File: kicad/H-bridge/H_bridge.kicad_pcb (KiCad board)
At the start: 2 copper layers, 127 x 63.5 mm, 69 parts, among them J1 Screw_Terminal_01x03, J2 Conn_Coaxial, J3 2453710000, J4 Screw_Terminal_01x02, Q1 IAUT300N10S5N014ATMA1, Q2 IAUT300N10S5N014ATMA1, Q3 IAUT300N10S5N014ATMA1, Q4 IAUT300N10S5N014ATMA1, U1 LTV-817, U2 PDS1-S15-S15-M, U3 HIP4080A, U4 LT1011, U5 LM340MPX-5.0/NOPB, U6 74LVC1G373, U8 74AC14DR

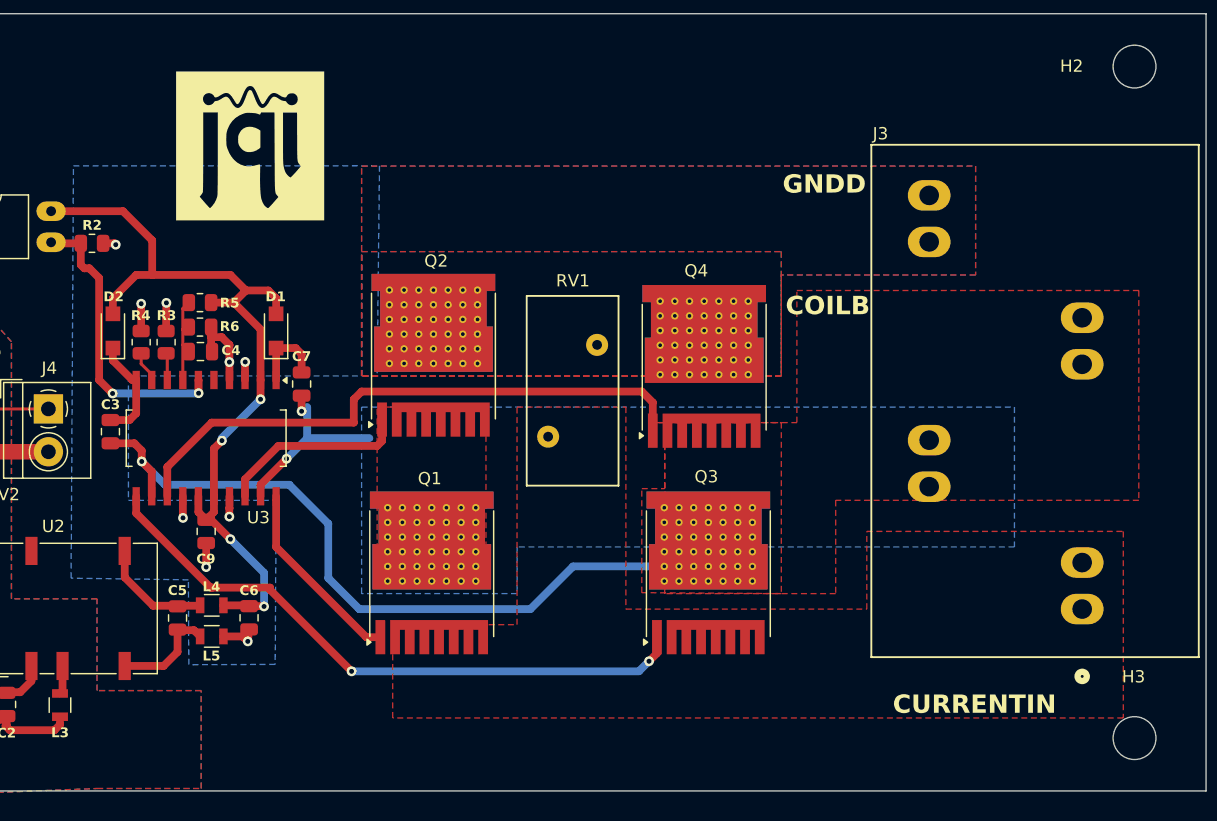
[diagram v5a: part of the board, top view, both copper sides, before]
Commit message: Fixed error is MOS package assigment and added solder mask for manual tin pour for increased conductivity
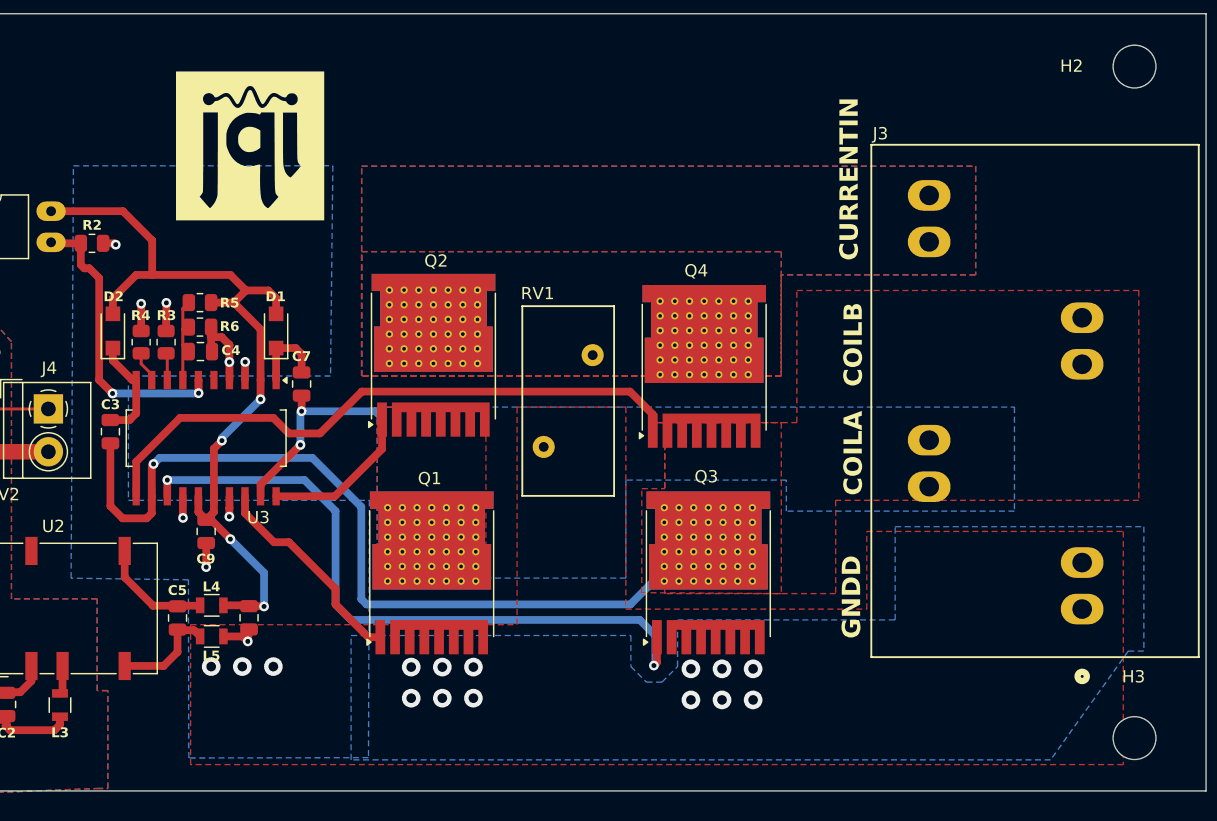
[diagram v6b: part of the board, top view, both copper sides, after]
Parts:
- moved RV1 7.59 mm to (178.5, 104.1), turned to -90 degrees
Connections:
- J3 pad 1: Current_in -> GNDD
- J3 pad 4: GNDD -> Current_in
- Q1 pad 2: Current_in -> GNDD
- Q2 pad 3: GNDD -> Current_in
- Q3 pad 2: Current_in -> GNDD
- Q4 pad 3: GNDD -> Current_in
- U3 pad 11: Net-(Q3-G) -> Net-(Q4-G)
- U3 pad 13: Net-(Q4-G) -> Net-(Q3-G)
- U3 pad 18: Net-(Q2-G) -> Net-(Q1-G)
- U3 pad 20: Net-(Q1-G) -> Net-(Q2-G)
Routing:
- net Coil_B: track 58.6 -> 70.7 mm
- net Net-(Q3-G): track 51.3 -> 55.8 mm
- net Net-(Q2-G): track 15.6 -> 12.7 mm
- net Net-(Q4-G): track 48.4 -> 50.6 mm
- net Net-(Q1-G): track 15.7 -> 17.4 mm
- net Coil_A: track 15.2 -> 16.4 mm
- net GNDD: vias 9 -> 24
- added copper zone on B.Cu, net Current_in
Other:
- board text added: "COILA"

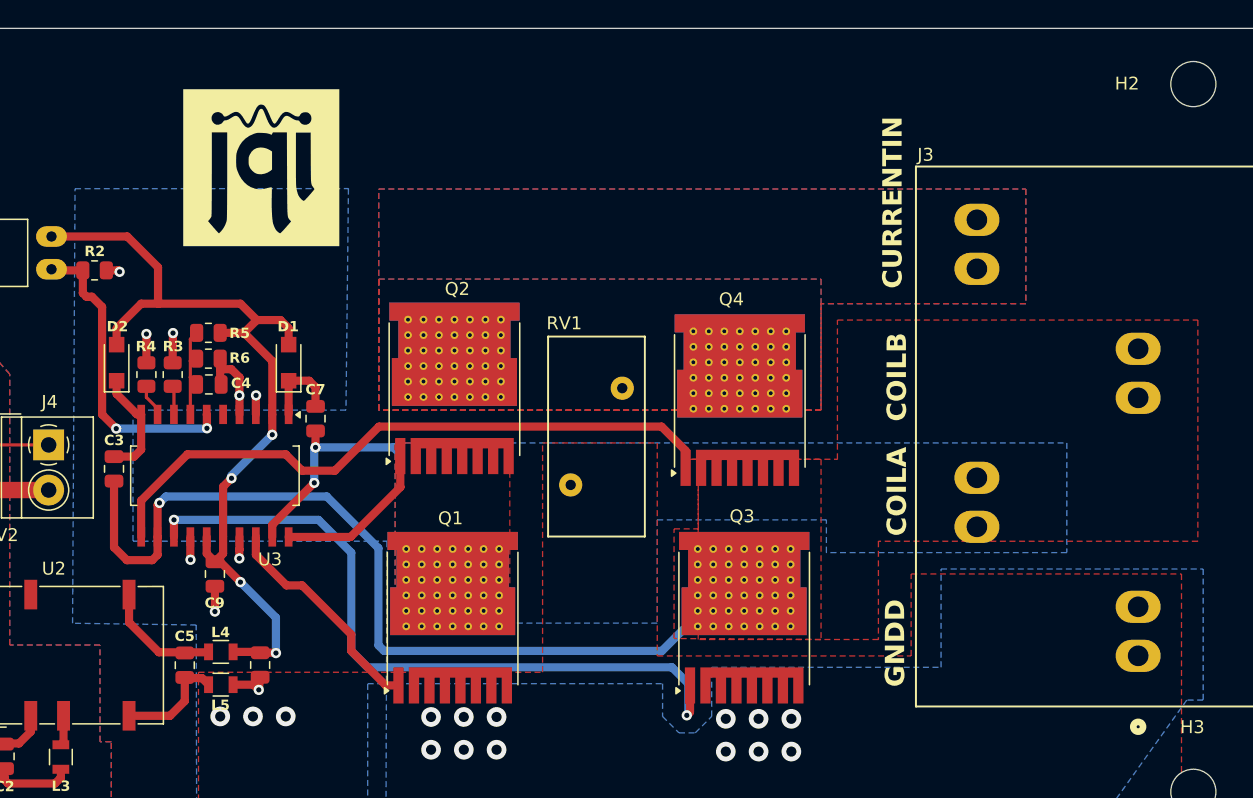
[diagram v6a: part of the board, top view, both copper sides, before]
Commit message: fixed connection error and added text
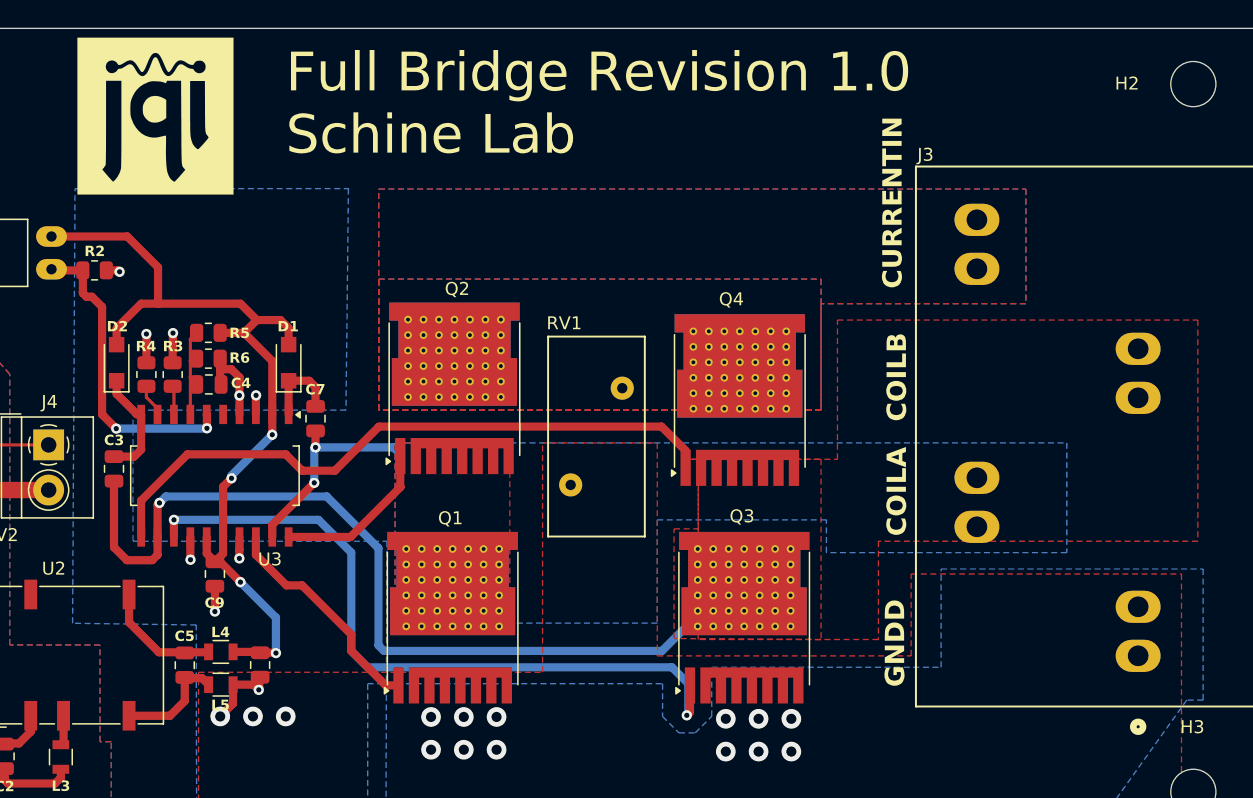
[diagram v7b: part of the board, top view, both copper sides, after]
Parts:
- moved LOGO_1 9.12 mm to (142.3, 83.0)
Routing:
- net GNDD: track 22.2 -> 25.1 mm
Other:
- board text added: "Full Bridge Revision 1.0 Schine Lab"
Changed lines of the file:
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@@
 			(psa4output no)
 			(plotreference yes)
-			(plotvalue yes)
+			(plotvalue no)
 			(plotfptext yes)
 			(plotinvisibletext no)
@@
 	(footprint "footprints:JQI-Logo"
 		(layer "F.Cu")
-		(at 150.5 87)
+		(at 142.3 83)
 		(property "Reference" "LOGO_1"
 			(at 0 0 0)
@@
 		(tags "varistor SIOV")
 		(property "Reference" "RV1"
-			(at -5.032921 4.496489 360)
+			(at -5.032921 4.496489 0)
 			(layer "F.SilkS")
 			(effects
@@
 		)
 	)
+	(gr_text "Full Bridge Revision 1.0\nSchine Lab "
+		(at 152.4 86.2 0)
+		(layer "F.SilkS")
+		(effects
+			(font
+				(size 3 3)
+				(thickness 0.15)
+			)
+			(justify left bottom)
+		)
+	)
 	(gr_text "COILA"
 		(at 200.66 115.57 90)
@@
 		)
 		(height 9.683539)
-		(gr_text "2499.2113 mils"
+		(gr_text "63.4800 mm"
 			(at 239.441301 107.937334 -89.98598654)
 			(layer "Dwgs.User")
@@
 		)
 		(height 7.210214)
-		(gr_text "5000.6113 mils"
+		(gr_text "127.0155 mm"
 			(at 165.108719 145.750197 0.009037191542)
 			(layer "Dwgs.User")
@@
 	)
 	(segment
+		(start 149.89061 127.075656)
+		(end 148.31661 127.075656)
+		(width 0.635)
+		(layer "F.Cu")
+		(net 3)
+	)
+	(segment
 		(start 150.098642 104.648799)
 		(end 150.08342 104.664021)
@@
 	)
 	(segment
+		(start 148.31661 128.54339)
+		(end 147.32 129.54)
+		(width 0.635)
+		(layer "F.Cu")
+		(net 3)
+	)
+	(segment
 		(start 146.90842 121.40842)
 		(end 146.90842 119.446656)
@@
 	)
 	(segment
-		(start 148.31661 127.075656)
-		(end 149.89061 127.075656)
-		(width 0.635)
-		(layer "F.Cu")
-		(net 3)
-	)
-	(segment
 		(start 145.00342 115.626656)
 		(end 145.00342 117.379708)
@@
 		(width 0.635)
 		(layer "F.Cu")
+		(net 3)
+	)
+	(segment
+		(start 148.31661 127.075656)
+		(end 148.31661 128.54339)
+		(width 0.635)
+		(layer "F.Cu")

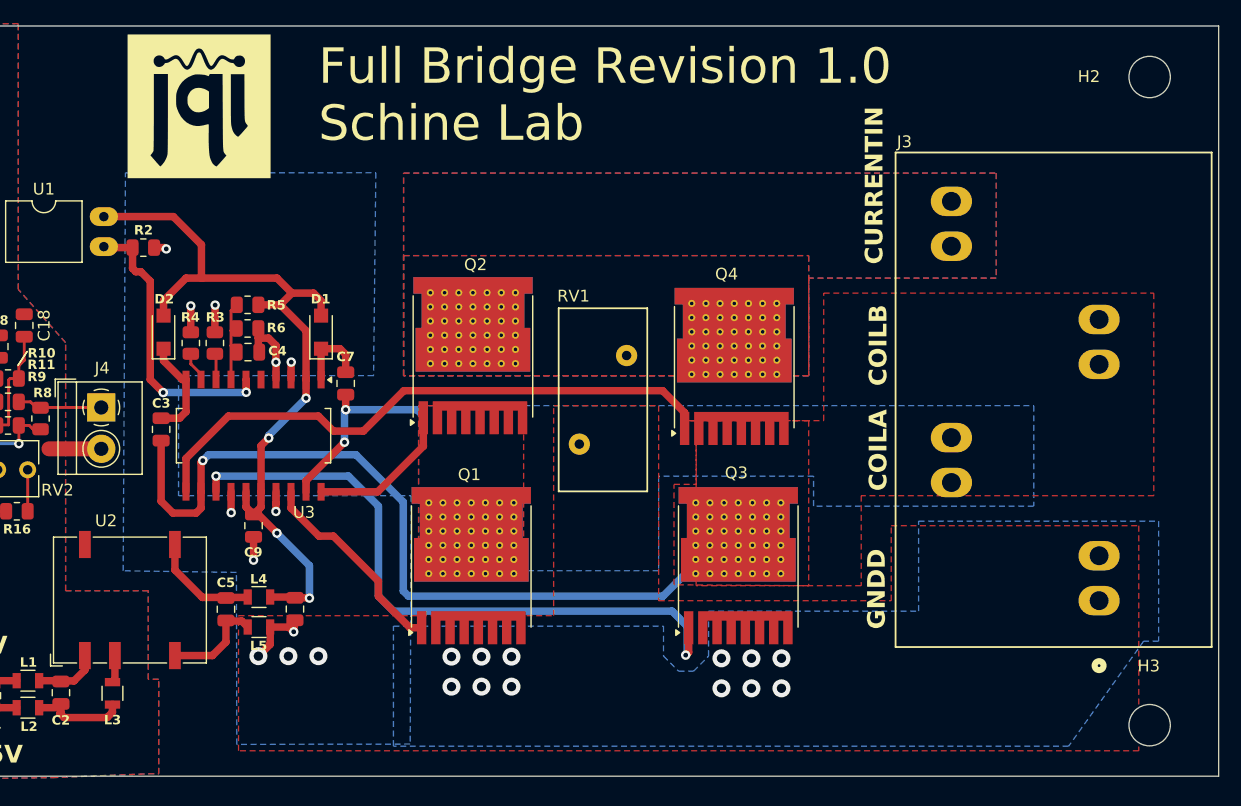
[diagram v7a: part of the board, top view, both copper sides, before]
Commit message: Aligned mountiing holes
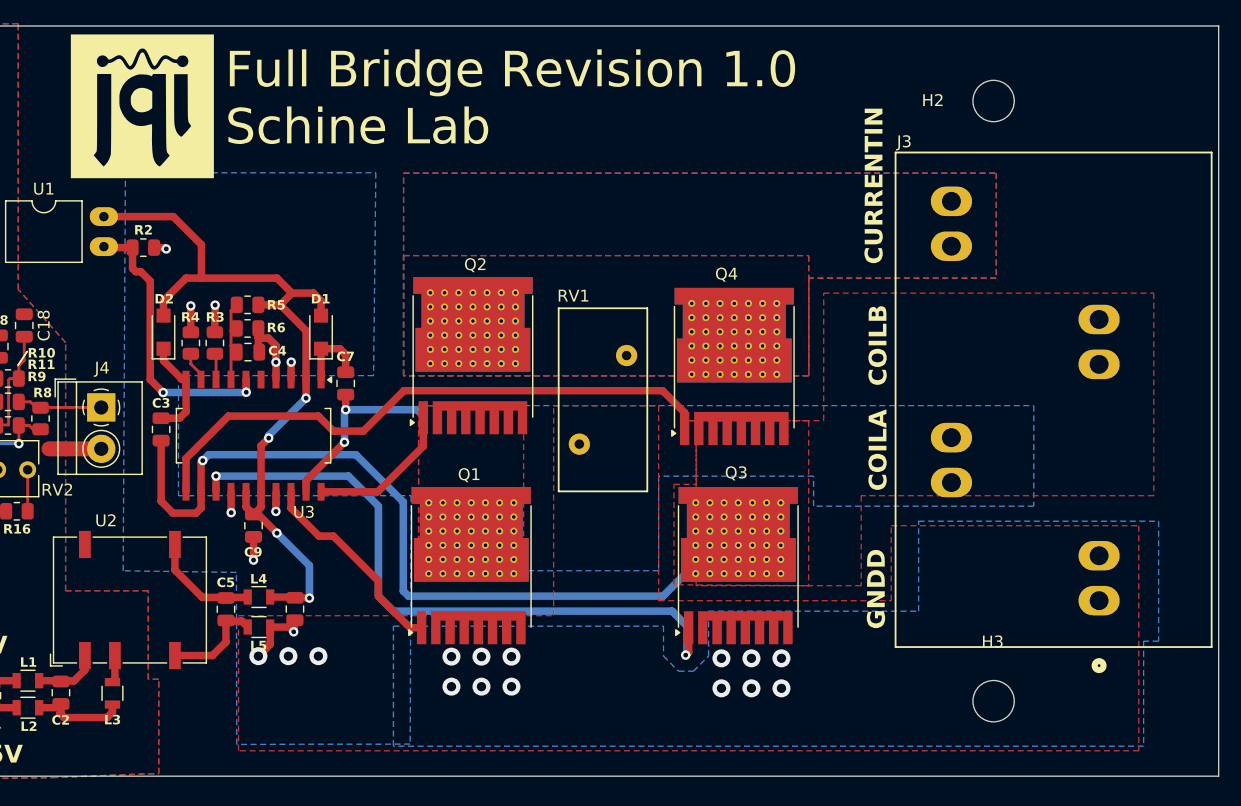
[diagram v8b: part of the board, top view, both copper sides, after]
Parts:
- moved H3 13.4 mm to (209.6, 133.3)
- moved H2 13.4 mm to (209.6, 82.5)
- moved LOGO_1 4.80 mm to (137.5, 83.0)
